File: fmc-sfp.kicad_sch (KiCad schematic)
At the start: 31 parts, among them J1 ASP-134604-01, J4 132134, J5 132134, J6 132134, J7 132134, U1 MAX9113EKA_TT, U2 MAX9113EKA_TT

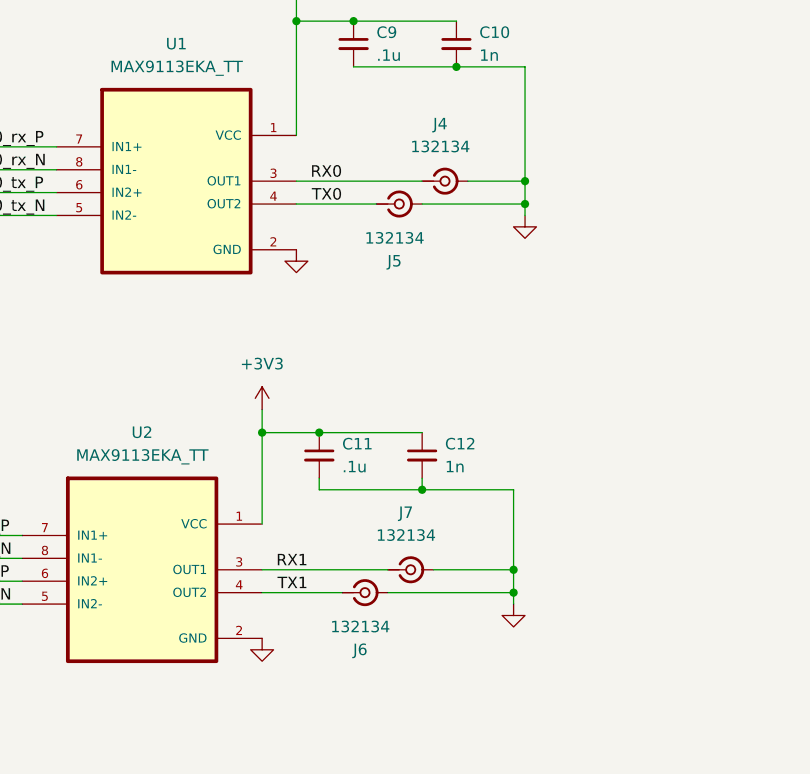
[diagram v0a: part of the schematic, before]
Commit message: Change part numbers for nextpcb
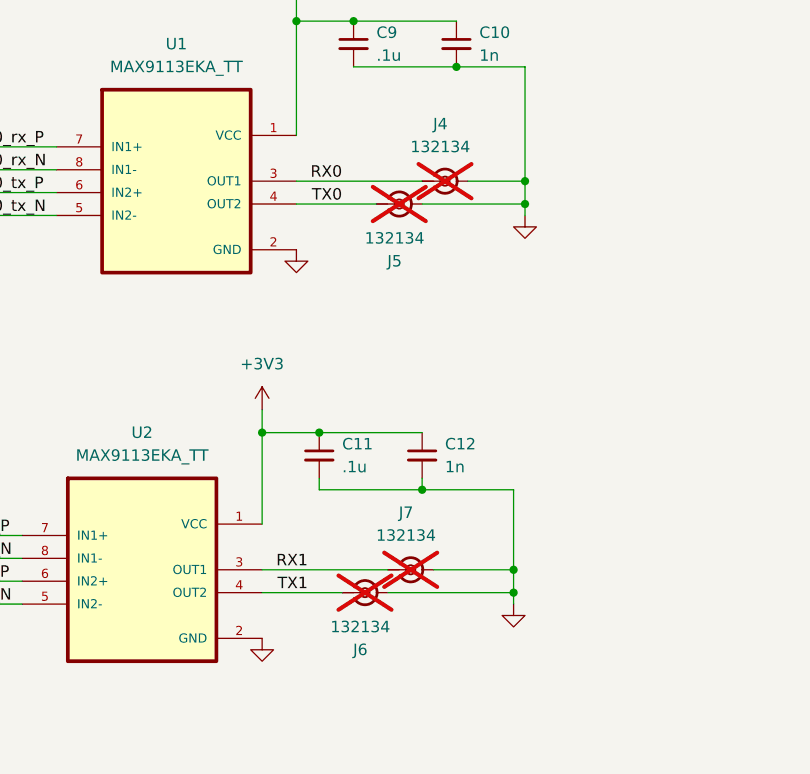
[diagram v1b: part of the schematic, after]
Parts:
- C1, C2, C3, C4, C5, C6, C7, C8: MANUFACTURER TDK Corporation -> Yageo; MPN C1608X7R1C105K080DC -> CC0603KRX7R6BB105
- C10, C12: MANUFACTURER KEMET -> Yageo; MPN C0603C102K5RAC7867 -> CC0603FRNPO8BN102
- C11, C9: MANUFACTURER KEMET -> Yageo; MPN C0603C104M5RAC7867 -> CC0603KRX7R7BB104
- J4, J5, J6, J7: now not fitted
- R11, R12, R13, R14, R2, R3, R4, R5: MANUFACTURER Bourns Inc. -> Yageo; MPN CR0603-FX-1002ELF -> RT0603BRE0710KL
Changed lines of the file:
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@@
 		(in_bom yes)
 		(on_board yes)
-		(dnp no)
+		(dnp yes)
 		(property "Reference" "J5"
 			(at 205.2204 118.11 0)
@@
 			)
 		)
-		(property "MANUFACTURER" "Bourns Inc."
+		(property "MANUFACTURER" "Yageo"
 			(at 50.8 171.45 0)
 			(effects
@@
 			)
 		)
-		(property "MPN" "CR0603-FX-1002ELF"
+		(property "MPN" "RT0603BRE0710KL"
 			(at 50.8 171.45 0)
 			(effects
@@
 			)
 		)
-		(property "MANUFACTURER" "TDK Corporation"
+		(property "MANUFACTURER" "Yageo"
 			(at 104.14 110.49 0)
 			(effects
@@
 			)
 		)
-		(property "MPN" "  C1608X7R1C105K080DC"
+		(property "MPN" "CC0603KRX7R6BB105"
 			(at 104.14 110.49 0)
 			(effects
@@
 			)
 		)
-		(property "MANUFACTURER" "KEMET"
+		(property "MANUFACTURER" "Yageo"
 			(at 196.85 139.7 0)
 			(effects
@@
 			)
 		)
-		(property "MPN" "C0603C104M5RAC7867"
+		(property "MPN" "CC0603KRX7R7BB104"
 			(at 196.85 139.7 0)
 			(effects
@@
 		(in_bom yes)
 		(on_board yes)
-		(dnp no)
+		(dnp yes)
 		(property "Reference" "J6"
 			(at 201.4104 161.29 0)
@@
 			)
 		)
-		(property "MANUFACTURER" "TDK Corporation"
+		(property "MANUFACTURER" "Yageo"
 			(at 97.79 102.87 0)
 			(effects
@@
 			)
 		)
-		(property "MPN" "  C1608X7R1C105K080DC"
+		(property "MPN" "CC0603KRX7R6BB105"
 			(at 97.79 102.87 0)
 			(effects
@@
 			)
 		)
-		(property "MANUFACTURER" "TDK Corporation"
+		(property "MANUFACTURER" "Yageo"
 			(at 104.14 168.91 0)
 			(effects
@@
 			)
 		)
-		(property "MPN" "  C1608X7R1C105K080DC"
+		(property "MPN" "CC0603KRX7R6BB105"
 			(at 104.14 168.91 0)
 			(effects
@@
 			)
 		)
-		(property "MANUFACTURER" "TDK Corporation"
+		(property "MANUFACTURER" "Yageo"
 			(at 97.79 158.75 0)
 			(effects
@@
 			)
 		)
-		(property "MPN" "  C1608X7R1C105K080DC"
+		(property "MPN" "CC0603KRX7R6BB105"
 			(at 97.79 158.75 0)
 			(effects
@@
 		(in_bom yes)
 		(on_board yes)
-		(dnp no)
+		(dnp yes)
 		(fields_autoplaced yes)
 		(property "Reference" "J7"
@@
 			)
 		)
-		(property "MANUFACTURER" "Bourns Inc."
+		(property "MANUFACTURER" "Yageo"
 			(at 35.56 99.06 0)
 			(effects
@@
 			)
 		)
-		(property "MPN" "CR0603-FX-1002ELF"
+		(property "MPN" "RT0603BRE0710KL"
 			(at 35.56 99.06 0)
 			(effects
@@
 			)
 		)
-		(property "MANUFACTURER" "TDK Corporation"
+		(property "MANUFACTURER" "Yageo"
 			(at 97.79 161.29 0)
 			(effects
@@
 			)
 		)
-		(property "MPN" "  C1608X7R1C105K080DC"
+		(property "MPN" "CC0603KRX7R6BB105"
 			(at 97.79 161.29 0)
 			(effects
@@
 			)
 		)
-		(property "MANUFACTURER" "Bourns Inc."
+		(property "MANUFACTURER" "Yageo"
 			(at 50.8 115.57 0)
 			(effects
@@
 			)
 		)
-		(property "MPN" "CR0603-FX-1002ELF"
+		(property "MPN" "RT0603BRE0710KL"
 			(at 50.8 115.57 0)
 			(effects
@@
 			)
 		)
-		(property "MANUFACTURER" "KEMET"
+		(property "MANUFACTURER" "Yageo"
 			(at 212.09 93.98 0)
 			(effects
@@
 			)
 		)
-		(property "MPN" "C0603C102K5RAC7867"
+		(property "MPN" "CC0603FRNPO8BN102"
 			(at 212.09 93.98 0)
 			(effects
@@
 			)
 		)
-		(property "MANUFACTURER" "Bourns Inc."
+		(property "MANUFACTURER" "Yageo"
 			(at 50.8 99.06 0)
 			(effects
@@
 			)
 		)
-		(property "MPN" "CR0603-FX-1002ELF"
+		(property "MPN" "RT0603BRE0710KL"
 			(at 50.8 99.06 0)
 			(effects
@@
 			)
 		)
-		(property "MANUFACTURER" "Bourns Inc."
+		(property "MANUFACTURER" "Yageo"
 			(at 35.56 115.57 0)
 			(effects
@@
 			)
 		)
-		(property "MPN" "CR0603-FX-1002ELF"
+		(property "MPN" "RT0603BRE0710KL"
 			(at 35.56 115.57 0)
 			(effects
@@
 		(in_bom yes)
 		(on_board yes)
-		(dnp no)
+		(dnp yes)
 		(fields_autoplaced yes)
 		(property "Reference" "J4"
@@
 			)
 		)
-		(property "MANUFACTURER" "TDK Corporation"
+		(property "MANUFACTURER" "Yageo"
 			(at 97.79 105.41 0)
 			(effects
@@
 			)
 		)
-		(property "MPN" "  C1608X7R1C105K080DC"
+		(property "MPN" "CC0603KRX7R6BB105"
 			(at 97.79 105.41 0)
 			(effects
@@
 			)
 		)
-		(property "MANUFACTURER" "TDK Corporation"
+		(property "MANUFACTURER" "Yageo"
 			(at 104.14 113.03 0)
 			(effects
@@
 			)
 		)
-		(property "MPN" "  C1608X7R1C105K080DC"
+		(property "MPN" "CC0603KRX7R6BB105"
 			(at 104.14 113.03 0)
 			(effects
@@
 			)
 		)
-		(property "MANUFACTURER" "KEMET"
+		(property "MANUFACTURER" "Yageo"
 			(at 200.66 93.98 0)
 			(effects
@@
 			)
 		)
-		(property "MPN" "C0603C104M5RAC7867"
+		(property "MPN" "CC0603KRX7R7BB104"
 			(at 200.66 93.98 0)
 			(effects
@@
 			)
 		)
-		(property "MANUFACTURER" "Bourns Inc."
+		(property "MANUFACTURER" "Yageo"
 			(at 35.56 171.45 0)
 			(effects
@@
 			)
 		)
-		(property "MPN" "CR0603-FX-1002ELF"
+		(property "MPN" "RT0603BRE0710KL"
 			(at 35.56 171.45 0)
 			(effects
@@
 			)
 		)
-		(property "MANUFACTURER" "TDK Corporation"
+		(property "MANUFACTURER" "Yageo"
 			(at 104.14 166.37 0)
 			(effects
@@
 			)
 		)
-		(property "MPN" "  C1608X7R1C105K080DC"
+		(property "MPN" "CC0603KRX7R6BB105"
 			(at 104.14 166.37 0)
 			(effects
@@
 			)
 		)
-		(property "MANUFACTURER" "KEMET"
+		(property "MANUFACTURER" "Yageo"
 			(at 208.28 139.7 0)
 			(effects
@@
 			)
 		)
-		(property "MPN" "C0603C102K5RAC7867"
+		(property "MPN" "CC0603FRNPO8BN102"
 			(at 208.28 139.7 0)
 			(effects
@@
 			)
 		)
-		(property "MANUFACTURER" "Bourns Inc."
+		(property "MANUFACTURER" "Yageo"
 			(at 50.8 154.94 0)
 			(effects
@@
 			)
 		)
-		(property "MPN" "CR0603-FX-1002ELF"
+		(property "MPN" "RT0603BRE0710KL"
 			(at 50.8 154.94 0)
 			(effects
@@
 			)
 		)
-		(property "MANUFACTURER" "Bourns Inc."
+		(property "MANUFACTURER" "Yageo"
 			(at 35.56 154.94 0)
 			(effects
@@
 			)
 		)
-		(property "MPN" "CR0603-FX-1002ELF"
+		(property "MPN" "RT0603BRE0710KL"
 			(at 35.56 154.94 0)
 			(effects

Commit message: change 0402 Resister for 0603 resistor
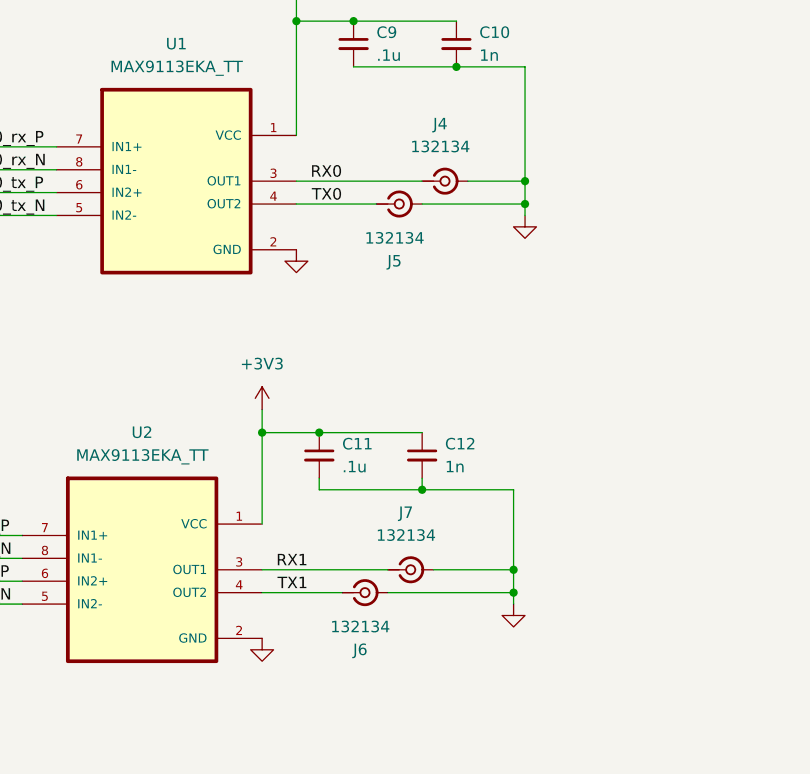
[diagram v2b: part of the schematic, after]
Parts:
- J4, J5, J6, J7: now fitted
- R1, R6: MPN RC0402FR-07100KL -> RC0603FR-07100KL
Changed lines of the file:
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@@
 		(in_bom yes)
 		(on_board yes)
-		(dnp yes)
+		(dnp no)
 		(property "Reference" "J5"
 			(at 205.2204 118.11 0)
@@
 		(in_bom yes)
 		(on_board yes)
-		(dnp yes)
+		(dnp no)
 		(property "Reference" "J6"
 			(at 201.4104 161.29 0)
@@
 		(in_bom yes)
 		(on_board yes)
-		(dnp yes)
+		(dnp no)
 		(fields_autoplaced yes)
 		(property "Reference" "J7"
@@
 			)
 		)
-		(property "MPN" "  RC0402FR-07100KL"
+		(property "MPN" "RC0603FR-07100KL"
 			(at 43.18 106.68 0)
 			(effects
@@
 		(in_bom yes)
 		(on_board yes)
-		(dnp yes)
+		(dnp no)
 		(fields_autoplaced yes)
 		(property "Reference" "J4"
@@
 			)
 		)
-		(property "MPN" "  RC0402FR-07100KL"
+		(property "MPN" "RC0603FR-07100KL"
 			(at 43.18 162.56 0)
 			(effects

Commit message: modify title block
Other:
- company: (none) -> MicroRidge Technology LTD
- title: (none) -> FMC-SFP
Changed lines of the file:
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@@
 	(generator_version "8.0")
 	(paper "A4")
+	(title_block
+		(title "FMC-SFP")
+		(date "2024-05-08")
+		(rev "Rev0")
+		(company "MicroRidge Technology LTD")
+	)
 	(junction
 		(at 205.74 64.77)
